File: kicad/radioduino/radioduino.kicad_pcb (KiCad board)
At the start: 2 copper layers, 130.5 x 70 mm, 48 parts, among them J1 Conn_01x03_Socket, J2 Conn_Coaxial_Small, J3 Conn_Coaxial_Small, J4 Conn_Coaxial_Small, J5 Conn_Coaxial_Small, J6 Conn_01x15, J7 Conn_01x15, Q1 SS8050, Q2 BSS138, Q3 BSS138, SW1 RotaryEncoder_Switch_MP, U1 PCF8574AT, U2 RT9193-33GB, Y1 Si5351A-B-GT

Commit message: pcb
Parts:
- removed REF** (x4): MountingHole_2.5mm_Pad, MountingHole:MountingHole_2.5mm_Pad
- added C7: 100n, Capacitor_SMD:C_0805_2012Metric, B.Cu at (191.0, 65.0)
- added C8: 100n, Capacitor_SMD:C_0805_2012Metric, B.Cu at (202.5, 64.5)
- added C9: 100n, Capacitor_SMD:C_0805_2012Metric, B.Cu at (211.5, 64.5)
- C1, C2, C3, C4, C5, C6, J2, J3, J4, J5, JP1, JP2, JP3, JP7, JP8, Q1, Q2, Q3, R1, R10, R11, R12, R2, R3, R4, R5, R6, R7, R8, R9, U1, U2, U3, Y1: moved to B.Cu
- JP4: moved to F.Cu
- moved RV1 97.5 mm to (186.0, 68.8)
- moved R4 75.4 mm to (76.5, 79.0), turned to 0 degrees
- moved R5 70.9 mm to (76.5, 81.5), turned to 0 degrees
- moved J7 47.0 mm to (80.0, 96.6), turned to 180 degrees
- moved JP4 44.2 mm to (76.2, 85.5), turned to 180 degrees
- moved J1 41.2 mm to (76.0, 89.5)
- moved JP5 40.5 mm to (72.0, 91.7)
- moved C5 36.3 mm to (170.9, 68.0), turned to 180 degrees
- moved J5 35.7 mm to (213.0, 59.4), turned to 90 degrees
- moved Y1 30.9 mm to (170.9, 74.0), turned to 180 degrees
- moved C4 29.7 mm to (171.1, 70.5)
- moved R12 29.4 mm to (202.0, 89.5), turned to -90 degrees
- moved C1 26.0 mm to (155.5, 67.0), turned to 0 degrees
- moved R3 25.8 mm to (152.5, 86.0)
- moved U2 25.8 mm to (158.9, 73.9), turned to 180 degrees
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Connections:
- Y1 pad 10: Net-(J3-In) -> Net-(Y1-CLK0)
- Y1 pad 6: Net-(J5-In) -> Net-(Y1-CLK2)
- Y1 pad 9: Net-(J4-In) -> Net-(Y1-CLK1)
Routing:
- net +5V: track 284.5 -> 210.8 mm, vias 5 -> 11
- net /vin: track 74.4 -> 13.3 mm, vias 1 -> 0
- net Net-(DS1-VO): track 31.3 -> 80.2 mm, vias 1 -> 3
- net Net-(Y1-CLK2): track 0.00 -> 46.7 mm
- net Net-(DS1-D7): track 47.0 -> 5.12 mm
- net Net-(DS1-D6): track 45.8 -> 4.59 mm
- net /scl: track 94.4 -> 134.9 mm, vias 3 -> 5
- net Net-(DS1-D5): track 44.2 -> 4.65 mm
- net Net-(Y1-CLK1): track 0.00 -> 37.9 mm
- net Net-(DS1-LED(-)): track 40.0 -> 3.11 mm
- net Net-(DS1-D4): track 41.2 -> 5.18 mm
- net /d8: track 113.6 -> 141.2 mm, vias 2 -> 0
- net Net-(Y1-CLK0): track 0.00 -> 26.7 mm
- net GND: track 334.1 -> 310.5 mm, vias 11 -> 26
- net Net-(DS1-E): track 55.4 -> 35.4 mm, vias 2 -> 0
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- added copper zone on B.Cu, net GND
- added copper zone on F.Cu, net GND
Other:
- board size 130.5 x 70 mm -> 149.5 x 45 mm

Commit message: before ldo
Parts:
- added REF**: MountingHole_3.2mm_M3_DIN965_Pad, MountingHole:MountingHole_3.2mm_M3_DIN965_Pad, F.Cu at (215.0, 79.5)
- added REF**: MountingHole_3.2mm_M3_DIN965_Pad, MountingHole:MountingHole_3.2mm_M3_DIN965_Pad, F.Cu at (75.0, 62.0)
- added REF**: Symbol_Danger_8x8mm_Copper, Symbol:Symbol_Danger_8x8mm_Copper, F.Cu at (91.0, 82.0)
- added REF**: Symbol_Barrel_Polarity, Symbol:Symbol_Barrel_Polarity, F.Cu at (71.5, 71.0)
- added REF**: MountingHole_3.2mm_M3_DIN965_Pad, MountingHole:MountingHole_3.2mm_M3_DIN965_Pad, F.Cu at (214.5, 97.0)
- added REF**: MountingHole_3.2mm_M3_DIN965_Pad, MountingHole:MountingHole_3.2mm_M3_DIN965_Pad, F.Cu at (75.0, 97.0)
- moved J1 21.1 mm to (74.0, 68.5)
- moved JP5 11.2 mm to (72.0, 80.5)
- moved JP4 3.51 mm to (76.3, 89.0)
- moved J2 0.71 mm to (216.1, 68.5)
- moved J5 0.71 mm to (213.5, 59.9)
- moved C9 0.55 mm to (211.5, 65.0)
- moved C8 0.50 mm to (202.5, 65.0)
- moved J3 0.50 mm to (190.5, 59.9)
- moved J4 0.50 mm to (202.0, 59.9)
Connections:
- Y1 pad 8: unconnected-(Y1-GND-Pad8) -> GND
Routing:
- net GND: track 310.5 -> 388.7 mm, vias 26 -> 27
- net +5V: track 210.8 -> 224.9 mm, vias 11 -> 10
- net +3.3V: track 47.9 -> 57.1 mm
- net /vin: track 13.3 -> 21.9 mm
- net Net-(J1-Pin_2): track 4.12 -> 11.3 mm
- net /d7: track 119.6 -> 124.9 mm
- net /5va: track 8.63 -> 3.78 mm
- net Net-(Q3-D): track 7.85 -> 10.9 mm
- net Net-(J5-In): track 4.76 -> 7.65 mm
- net /d6: track 127.1 -> 129.3 mm
- net /d8: track 141.2 -> 142.8 mm
- net /sda: track 106.7 -> 106.0 mm
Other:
- board text added: "+"
- board text added: "Attention pirates inside"
- board text added: "clk 0"
- board text added: "clk 1"
- board text added: "clk 2"
- board text added: "contrast"
- board text added: "external refrance 10 - 100Mhz"
- board text added: "|"

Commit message: 
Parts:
- added C10: 10u, Capacitor_SMD:C_0805_2012Metric, B.Cu at (94.5, 75.5)
- added C11: 10u, Capacitor_SMD:C_0805_2012Metric, B.Cu at (94.0, 64.5)
- added JP9: SolderJumper_2_Open, Jumper:SolderJumper-2_P1.3mm_Open_TrianglePad1.0x1.5mm, B.Cu at (90.8, 75.5)
- added U4: NCP1117-5.0_SOT223, Package_TO_SOT_SMD:SOT-223-3_TabPin2, B.Cu at (91.0, 70.0)
- moved JP5 1.00 mm to (73.0, 80.5)
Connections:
- JP5 pad 2: Net-(J1-Pin_2) -> Net-(JP5-C)
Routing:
- net Net-(JP5-C): track 0.00 -> 44.2 mm, vias 0 -> 1
- net GND: track 388.7 -> 410.4 mm, vias 27 -> 33
- net Net-(J1-Pin_2): track 11.3 -> 32.7 mm
- net +3.3V: track 57.1 -> 56.4 mm
- net +5V: track 224.9 -> 224.2 mm
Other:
- board text added: "Radioduino YO3DBZ & YO3FLX"

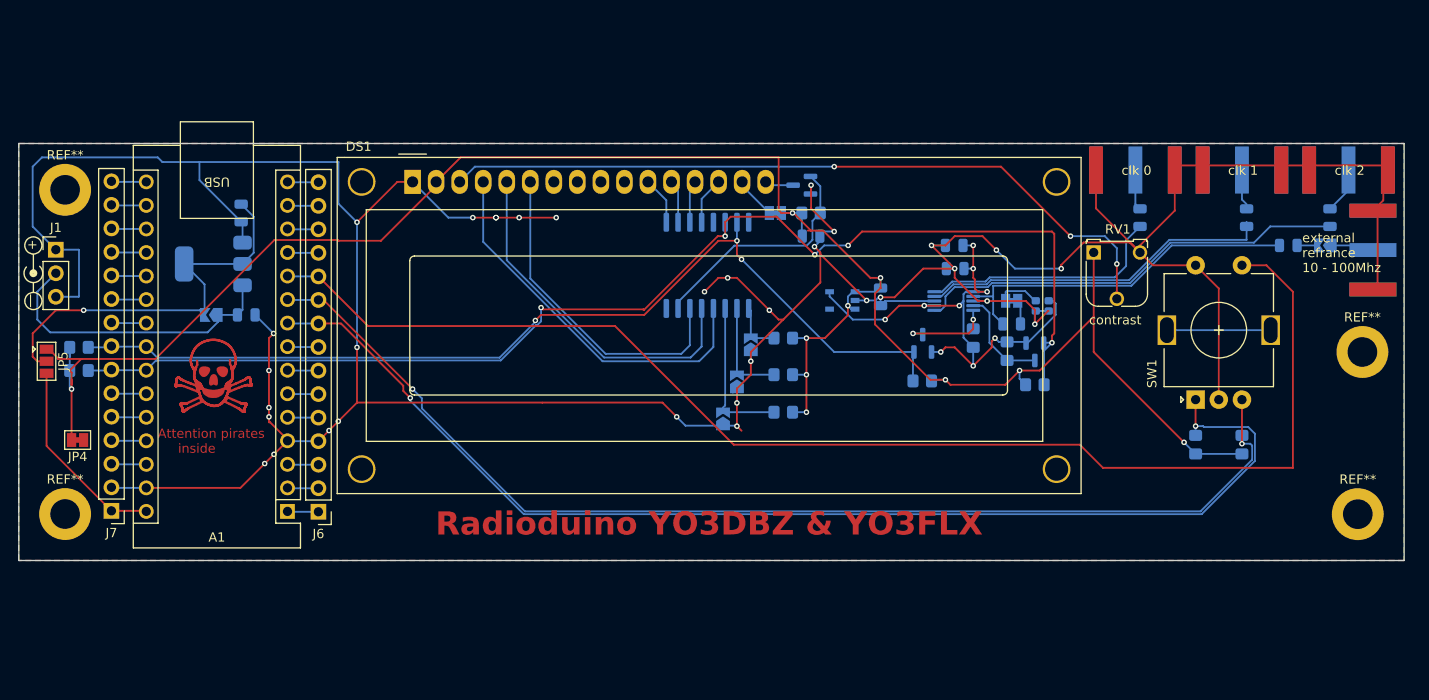
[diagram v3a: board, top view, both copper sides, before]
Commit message: fixed pcb added encoder for rit
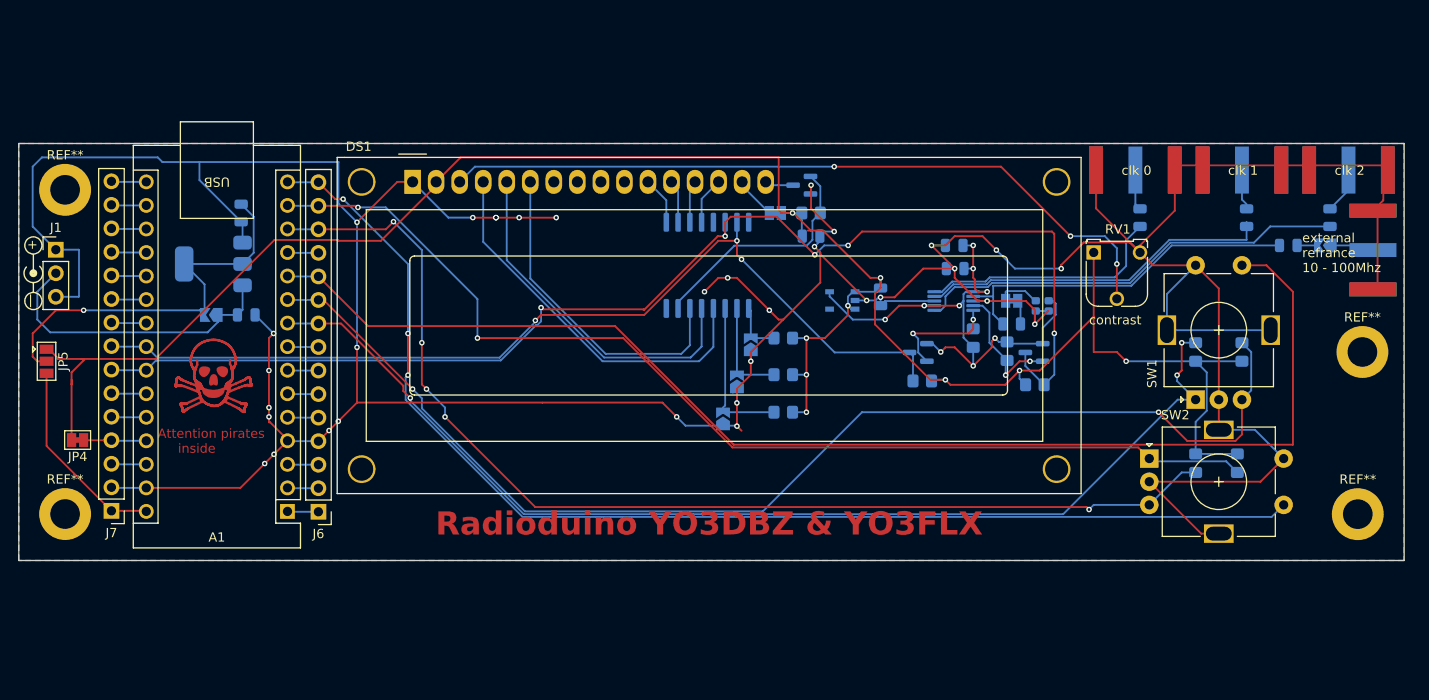
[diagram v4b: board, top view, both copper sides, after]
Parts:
- removed R4, R5: 4.7K, Resistor_SMD:R_0805_2012Metric_Pad1.20x1.40mm_HandSolder
- added R13: 10K, Resistor_SMD:R_0805_2012Metric_Pad1.20x1.40mm_HandSolder, B.Cu at (201.5, 91.5)
- added R14: 10K, Resistor_SMD:R_0805_2012Metric_Pad1.20x1.40mm_HandSolder, B.Cu at (197.0, 91.5)
- added SW2: RotaryEncoder_Switch_MP, Rotary_Encoder:RotaryEncoder_Alps_EC11E-Switch_Vertical_H20mm, F.Cu at (192.0, 91.0)
- moved R11 10.0 mm to (197.0, 79.5)
- moved R12 10.0 mm to (202.0, 79.5)
- moved Q3 1.10 mm to (167.1, 79.5), turned to 180 degrees
- moved Q2 0.12 mm to (179.6, 79.5), turned to 180 degrees
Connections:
- Q2 pad 2: /scl -> Net-(Q2-S)
- Q2 pad 3: Net-(Q2-D) -> /scl
- Q3 pad 2: /sda -> Net-(Q3-S)
- Q3 pad 3: Net-(Q3-D) -> /sda
- R10 pad 2: Net-(Q3-D) -> Net-(Q3-S)
- R9 pad 2: Net-(Q2-D) -> Net-(Q2-S)
- SW1 pad MP: unconnected-(SW1-PadMP) -> GND
- Y1 pad 4: Net-(Q2-D) -> Net-(Q2-S)
- Y1 pad 5: Net-(Q3-D) -> Net-(Q3-S)
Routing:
- net /d12: track 3.36 -> 132.0 mm, vias 0 -> 3
- net /d10: track 3.36 -> 122.0 mm, vias 0 -> 5
- net /d11: track 3.36 -> 116.9 mm, vias 0 -> 2
- net GND: track 410.4 -> 466.8 mm
- net Net-(Q2-S): track 0.00 -> 14.3 mm, vias 0 -> 2
- net Net-(Q3-S): track 0.00 -> 13.3 mm, vias 0 -> 2
- net unconnected-(SW1-PadMP): track 11.2 -> 0.00 mm
- net Net-(Q2-D): track 11.0 -> 0.00 mm
- net Net-(Q3-D): track 10.9 -> 0.00 mm, vias 2 -> 0
- net /d6: track 129.3 -> 120.8 mm, vias 2 -> 3
- net +5V: track 224.2 -> 229.9 mm, vias 10 -> 9
- net /d7: track 124.9 -> 129.8 mm
- net /d8: track 142.8 -> 139.2 mm
- net /5va: track 3.78 -> 6.79 mm
- net /sda: track 106.0 -> 103.3 mm
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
